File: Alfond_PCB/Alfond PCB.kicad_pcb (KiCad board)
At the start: 4 copper layers, 39 parts, among them J3 Conn_01x05_Pin, J5 USB_B_Micro, P1 PHR-2, SW1 SW_SPDT, U1 DS18B20, U2 STM32U545VETx, U3 MIC5219-3.3YMM, Y1 16MHz

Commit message: Add files via upload
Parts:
- added INA+: PinHeader_1x01_P2.54mm_Vertical, Connector_PinHeader_2.54mm:PinHeader_1x01_P2.54mm_Vertical, F.Cu at (180.5, 77.5)
- added INA-: PinHeader_1x01_P2.54mm_Vertical, Connector_PinHeader_2.54mm:PinHeader_1x01_P2.54mm_Vertical, F.Cu at (186.5, 77.5)
- moved C1 16.3 mm to (224.0, 89.5), turned to 180 degrees
- moved C7 4.03 mm to (214.0, 66.5), turned to -90 degrees
- moved C13 2.00 mm to (174.0, 89.0)
- moved C6 1.50 mm to (212.5, 70.5)
- moved C4 1.12 mm to (213.5, 78.5)
- moved R5 0.50 mm to (221.0, 63.0)
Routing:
- net +3.3V: track 64.8 -> 267.5 mm, vias 1 -> 11
- net GND: track 222.6 -> 320.3 mm, vias 6 -> 12
- net /I2C1_SDA: track 0.00 -> 75.3 mm, vias 0 -> 3
- net /I2C1_SCL: track 0.00 -> 75.0 mm, vias 0 -> 3
- net /UART5_RX: track 0.00 -> 70.9 mm, vias 0 -> 1
- net /UART5_TX: track 0.00 -> 69.4 mm, vias 0 -> 3
- net /GPIO_SLEEP_XBEE: track 0.00 -> 60.2 mm, vias 0 -> 3
- net /UART4_TX: track 0.00 -> 41.7 mm, vias 0 -> 2
- net /INA+: track 0.00 -> 32.6 mm, vias 0 -> 3
- net /I2C3_SDA: track 0.00 -> 28.5 mm, vias 0 -> 4
- net /I2C3_SCL: track 0.00 -> 27.9 mm, vias 0 -> 2
- net /INA-: track 0.00 -> 27.3 mm, vias 0 -> 2
- net /NRST: track 47.9 -> 61.2 mm, vias 3 -> 4
- net Net-(D4-A): track 10.9 -> 15.0 mm, vias 0 -> 1
- net /GPIO_INPUT_Button: track 13.1 -> 15.0 mm
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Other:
- board outline added: 84.5 x 50 mm

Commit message: Removed layers
Had extra copper layers that weren't used, and forgot to comment on the last push, but it was creating a fully connected pcb
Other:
- copper layers 4 -> 2
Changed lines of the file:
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@@
 	(layers
 		(0 "F.Cu" signal)
-		(1 "In1.Cu" signal)
-		(2 "In2.Cu" signal)
 		(31 "B.Cu" power)
 		(34 "B.Paste" user)
@@
 			)
 			(layer "dielectric 1"
-				(type "prepreg")
-				(thickness 0.1)
-				(material "FR4")
-				(epsilon_r 4.5)
-				(loss_tangent 0.02)
-			)
-			(layer "In1.Cu"
-				(type "copper")
-				(thickness 0.035)
-			)
-			(layer "dielectric 2"
-				(type "prepreg")
-				(thickness 1.24)
-				(material "FR4")
-				(epsilon_r 4.5)
-				(loss_tangent 0.02)
-			)
-			(layer "In2.Cu"
-				(type "copper")
-				(thickness 0.035)
-			)
-			(layer "dielectric 3"
-				(type "prepreg")
-				(thickness 0.1)
+				(type "core")
+				(thickness 1.51)
 				(material "FR4")
 				(epsilon_r 4.5)
@@
 			(plot_on_all_layers_selection 0x0000000_00000000)
 			(disableapertmacros no)
-			(usegerberextensions no)
+			(usegerberextensions yes)
 			(usegerberattributes yes)
 			(usegerberadvancedattributes yes)
-			(creategerberjobfile yes)
+			(creategerberjobfile no)
 			(dashed_line_dash_ratio 12.000000)
 			(dashed_line_gap_ratio 3.000000)
@@
 			(plotinvisibletext no)
 			(sketchpadsonfab no)
-			(subtractmaskfromsilk no)
+			(subtractmaskfromsilk yes)
 			(outputformat 1)
 			(mirror no)
-			(drillshape 1)
+			(drillshape 0)
 			(scaleselection 1)
-			(outputdirectory "")
+			(outputdirectory "C:/Users/mpica/Downloads/Gerber_Files_Alfond_PCB/")
 		)
 	)

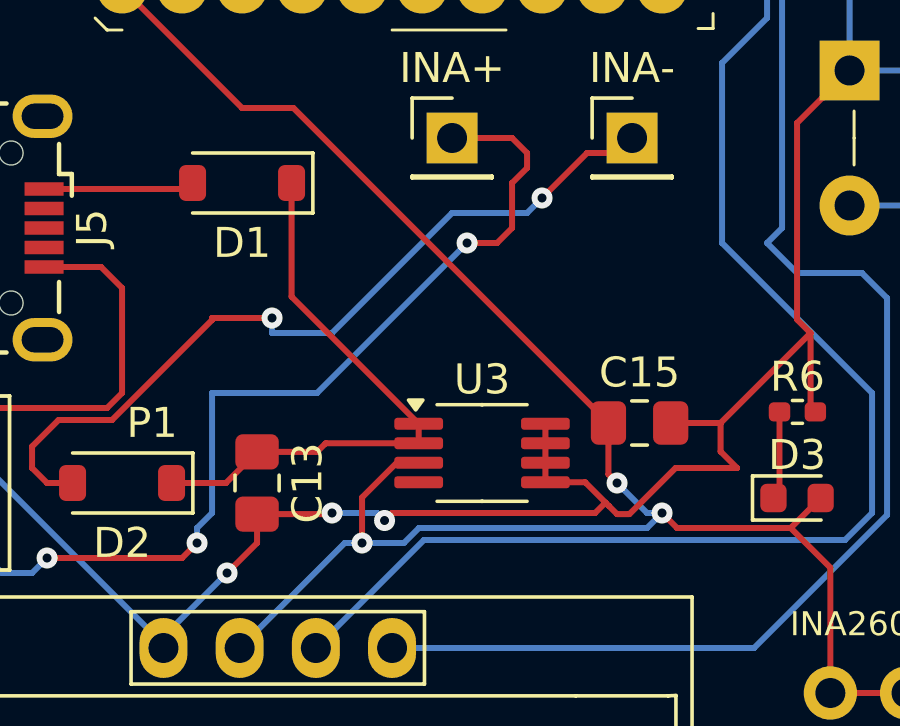
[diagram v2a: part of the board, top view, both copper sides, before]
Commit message: Update to PCB and Footprints
The PCB was updated to the correct MIC ordered from Digikey, and the footprint was added to the footprint folders.
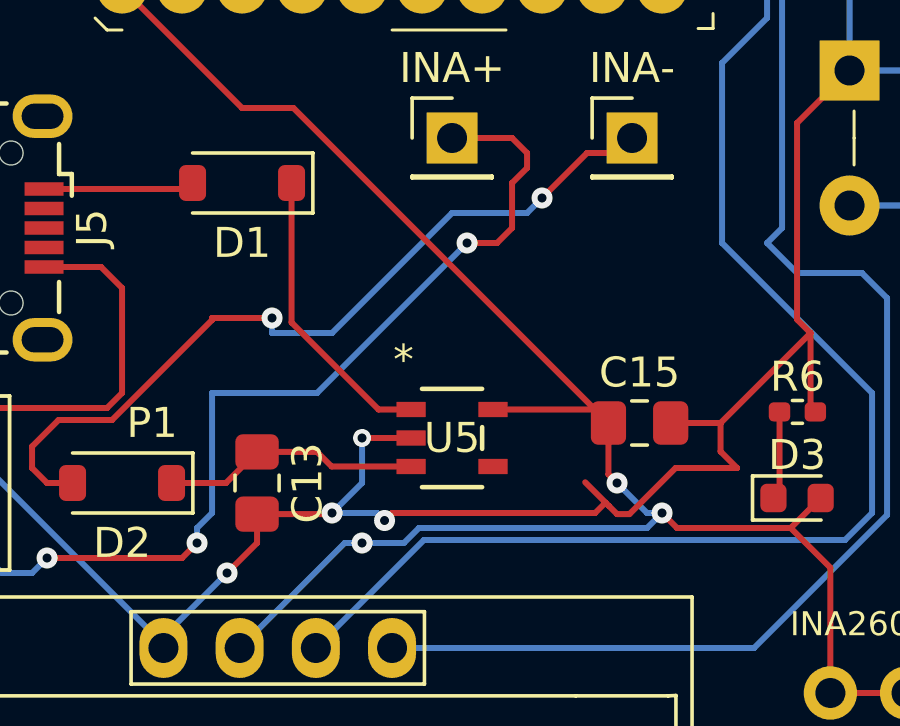
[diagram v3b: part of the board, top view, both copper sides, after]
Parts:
- removed U3: MIC5219-3.3YMM, Package_SO:MSOP-8_3x3mm_P0.65mm
- added U5: MIC5219-3.3YM5-TR, Mics:SOT-23-5_M5_MCH, F.Cu at (180.5, 87.5)
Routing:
- net GND: track 320.3 -> 321.6 mm, vias 12 -> 13
- net Net-(D1-K): track 19.2 -> 18.5 mm

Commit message: fixed few errors
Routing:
- net GND: track 321.6 -> 320.7 mm
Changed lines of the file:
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@@
 		(tags "MIC5219-3.3YM5-TR ")
 		(property "Reference" "U5"
-			(at 0 0 0)
+			(at 0 -3 0)
 			(unlocked yes)
 			(layer "F.SilkS")
@@
 		)
 		(fp_text user "*"
-			(at -1.61925 -2.601 0)
-			(layer "F.SilkS")
-			(effects
-				(font
-					(size 1 1)
-					(thickness 0.15)
-				)
-			)
-		)
-		(fp_text user "*"
-			(at -1.61925 -2.601 0)
-			(unlocked yes)
-			(layer "F.SilkS")
-			(effects
-				(font
-					(size 1 1)
-					(thickness 0.15)
-				)
-			)
-		)
-		(fp_text user "*"
 			(at -0.6223 -1.5088 0)
 			(unlocked yes)
@@
 		)
 		(pad "" smd roundrect
-			(at -0.3625 0)
+			(at -0.5 0)
 			(size 0.41 0.27)
 			(layers "F.Paste")
@@
 		)
 		(pad "" smd roundrect
-			(at 0.3625 0)
+			(at 0.5 0)
 			(size 0.41 0.27)
 			(layers "F.Paste")
@@
 		)
 		(pad "1" smd roundrect
-			(at -0.3375 0)
+			(at -0.5 0)
 			(size 0.575 0.3)
 			(layers "F.Cu" "F.Mask")
@@
 		)
 		(pad "2" smd roundrect
-			(at 0.3375 0)
+			(at 0.5 0)
 			(size 0.575 0.3)
 			(layers "F.Cu" "F.Mask")
@@
 	)
 	(segment
+		(start 189.45 87.95)
+		(end 189.45 87)
+		(width 0.2)
+		(layer "F.Cu")
+		(net 2)
+	)
+	(segment
 		(start 214 67.0675)
 		(end 214 68.39)
@@
 	)
 	(segment
+		(start 186 90.0375)
+		(end 186.4125 90.0375)
+		(width 0.2)
+		(layer "F.Cu")
+		(net 2)
+	)
+	(segment
 		(start 212.734 93.734)
 		(end 213 94)
@@
 	)
 	(segment
+		(start 185.615625 89.653125)
+		(end 186 90.0375)
+		(width 0.2)
+		(layer "F.Cu")
+		(net 2)
+	)
+	(segment
 		(start 216.325 77)
 		(end 218.5 77)
@@
 	)
 	(segment
-		(start 186.4125 90.0375)
-		(end 187.95 88.5)
-		(width 0.2)
-		(layer "F.Cu")
-		(net 2)
-	)
-	(segment
 		(start 226.248529 92.1)
 		(end 224.1 92.1)
@@
 	)
 	(segment
+		(start 186.4125 90.0375)
+		(end 187.95 88.5)
+		(width 0.2)
+		(layer "F.Cu")
+		(net 2)
+	)
+	(segment
 		(start 185.615625 89.653125)
 		(end 185.26875 90)
@@
 	)
 	(segment
-		(start 187.95 88.5)
-		(end 190 88.5)
-		(width 0.2)
-		(layer "F.Cu")
-		(net 2)
-	)
-	(segment
 		(start 229.4325 84.5)
 		(end 229.4325 88.418971)
@@
 	)
 	(segment
-		(start 190 88.5)
-		(end 189.45 87.95)
-		(width 0.2)
-		(layer "F.Cu")
-		(net 2)
-	)
-	(segment
 		(start 194 58.5)
 		(end 194 58)
@@
 	)
 	(segment
+		(start 216 93)
+		(end 214.8375 93)
+		(width 0.2)
+		(layer "F.Cu")
+		(net 2)
+	)
+	(segment
 		(start 210.5 77.365)
 		(end 211.0675 77.9325)
@@
 	)
 	(segment
-		(start 216 93)
-		(end 214.8375 93)
-		(width 0.2)
-		(layer "F.Cu")
-		(net 2)
-	)
-	(segment
-		(start 184.9375 88.975)
-		(end 185.73125 89.76875)
+		(start 218 80.34259)
+		(end 218 80)
 		(width 0.2)
 		(layer "F.Cu")
@@
 	)
 	(segment
-		(start 218 80.34259)
-		(end 218 80)
+		(start 174 90.0375)
+		(end 176.4625 90.0375)
 		(width 0.2)
 		(layer "F.Cu")
@@
 	)
 	(segment
-		(start 174 90.0375)
-		(end 176.4625 90.0375)
+		(start 187.95 88.5)
+		(end 190 88.5)
 		(width 0.2)
 		(layer "F.Cu")
@@
 	)
 	(segment
-		(start 189.45 87.95)
-		(end 189.45 87)
-		(width 0.2)
-		(layer "F.Cu")
-		(net 2)
-	)
-	(segment
 		(start 192.61 86.63)
 		(end 192.45 86.47)
@@
 	)
 	(segment
-		(start 185.73125 89.76875)
-		(end 186 90.0375)
-		(width 0.2)
-		(layer "F.Cu")
-		(net 2)
-	)
-	(segment
 		(start 174 91)
 		(end 173 92)
@@
 	)
 	(segment
-		(start 186 90.0375)
-		(end 186.4125 90.0375)
-		(width 0.2)
-		(layer "F.Cu")
-		(net 2)
-	)
-	(segment
 		(start 220.5 75)
 		(end 220.5 76)
@@
 		(net 2)
 	)
+	(segment
+		(start 190 88.5)
+		(end 189.45 87.95)
+		(width 0.2)
+		(layer "F.Cu")
+		(net 2)
+	)
 	(via
 		(at 194 58.5)
@@
 	(via
 		(at 177.5 87.5)
-		(size 0.6)
+		(size 0.7)
 		(drill 0.3)
 		(layers "F.Cu" "B.Cu")
@@
 	)
 	(segment
-		(start 213.9025 89.5)
-		(end 212.5 90.9025)
+		(start 215 87)
+		(end 215 84.675)
 		(width 0.2)
 		(layer "F.Cu")
@@
 	)
 	(segment
-		(start 215 87)
-		(end 215 84.675)
+		(start 215 88.4025)
+		(end 213.9025 89.5)
 		(width 0.2)
 		(layer "F.Cu")
@@
 	)
 	(segment
-		(start 215 88.4025)
-		(end 213.9025 89.5)
+		(start 213.9025 89.5)
+		(end 212.5 90.9025)
 		(width 0.2)
 		(layer "F.Cu")
@@
 	)
 	(segment
-		(start 212.5 92.5)
-		(end 213 93)
-		(width 0.2)
+		(start 213 93)
+		(end 214.1625 93)
+		(width 0.3)
 		(layer "F.Cu")
 		(net 5)
 	)
 	(segment
-		(start 213 93)
-		(end 214.1625 93)
-		(width 0.2)
+		(start 212.5 92.5)
+		(end 213 93)
+		(width 0.3)
 		(layer "F.Cu")
 		(net 5)

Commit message: PCB changes
Added text for project name and group members, along with changing capacitor 14 from a footprint that wasn't working with one that is.
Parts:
- C14: value 0.1u -> 100n; footprint Capacitor_SMD:C_01005_0402Metric_Pad0.57x0.30mm_HandSolder -> Capacitor_SMD:C_0402_1005Metric_Pad0.74x0.62mm_HandSolder
- moved C7 2.06 mm to (216.0, 66.0)
- moved C6 2.00 mm to (214.5, 70.5)
- moved C5 1.15 mm to (214.0, 72.5), turned to 180 degrees
- moved C4 1.12 mm to (214.5, 78.0)
- moved C2 1.00 mm to (230.0, 83.5)
- moved C9 0.50 mm to (234.5, 69.0), turned to 0 degrees
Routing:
- net GND: track 320.7 -> 334.0 mm
- net +3.3V: track 267.6 -> 259.5 mm, vias 11 -> 10
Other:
- board text added: "Alfond Data Logger Siddhartha Bajracharya Alex Picard"

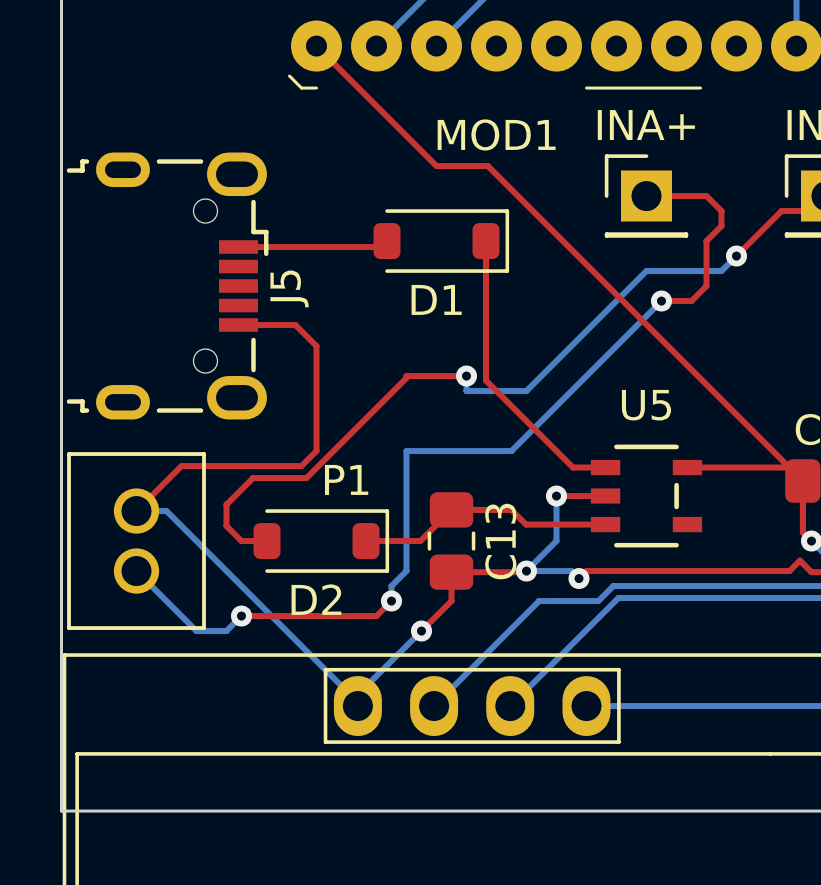
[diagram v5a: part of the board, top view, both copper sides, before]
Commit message: Final PCB Changes
Changed the Schottky diodes to the MAX40200 diodes
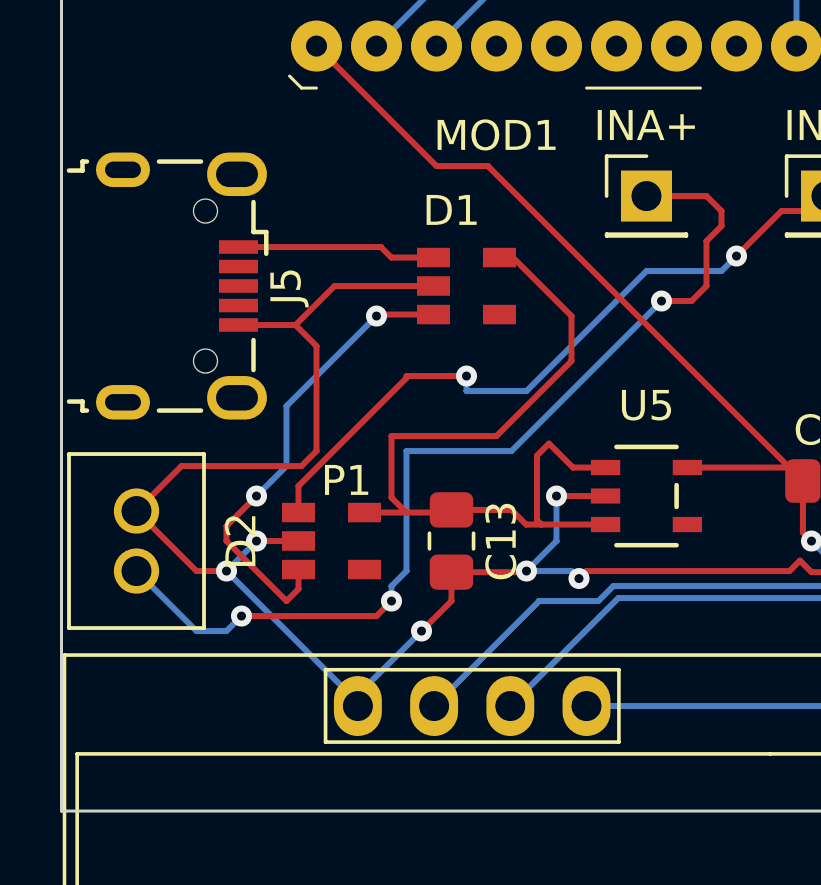
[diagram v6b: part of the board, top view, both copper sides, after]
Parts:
- D1, D2: value D_Schottky -> SOT-23-5; footprint Diode_SMD:D_SOD-123 -> MAX40200AUK_T:SOT-23-5
- moved D1 1.80 mm to (174.5, 80.5), turned to 90 degrees
- moved D2 0.50 mm to (170.0, 89.0), turned to 90 degrees
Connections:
- D1 pad 1: Net-(D1-K) -> /V_USB
- D1 pad 2: /V_USB -> GND
- D2 pad 1: Net-(D1-K) -> /INA-
- D2 pad 2: /INA- -> GND
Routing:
- net EN: track 0.00 -> 15.5 mm, vias 0 -> 2
- net Net-(D1-K): track 18.5 -> 27.9 mm
- net GND: track 334.0 -> 342.0 mm, vias 13 -> 15
- net /INA-: track 27.3 -> 23.2 mm
- net /V_USB: track 5.03 -> 6.64 mm

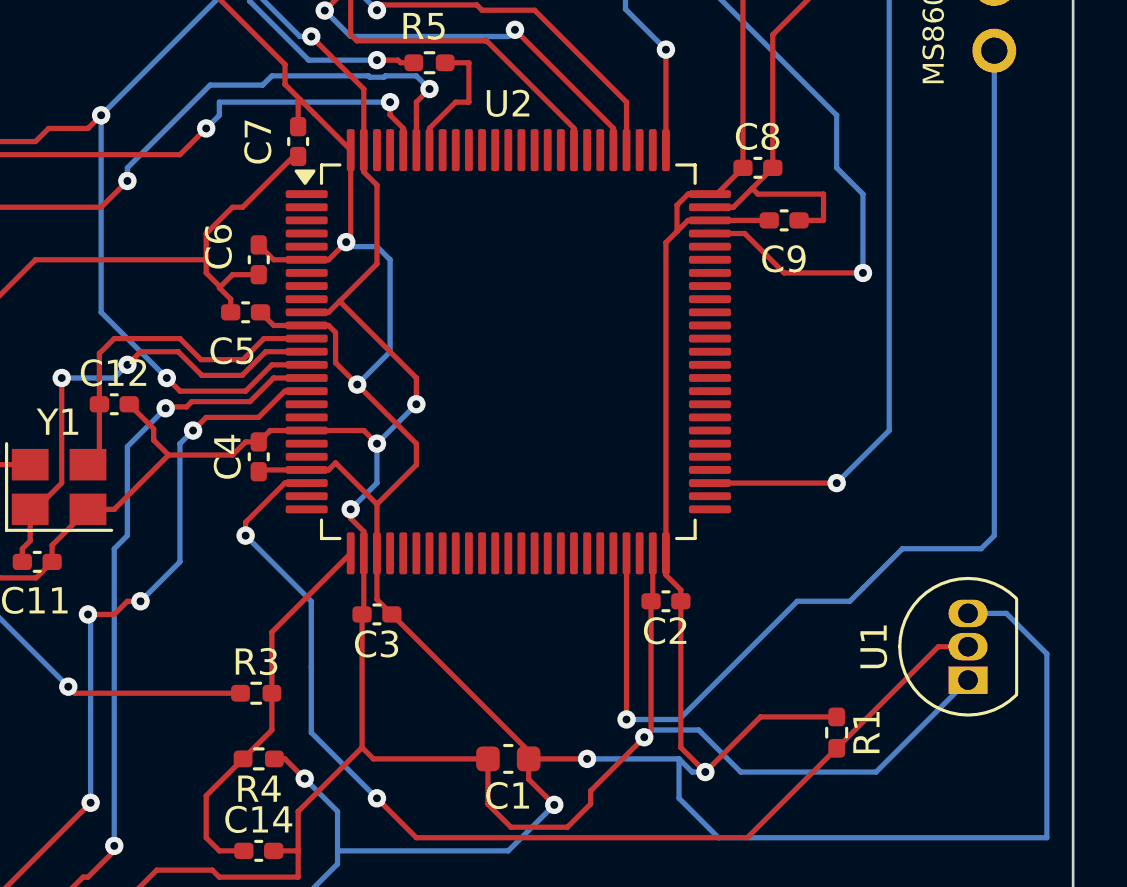
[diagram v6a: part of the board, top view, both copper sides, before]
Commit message: Added test points
Added test points for possible debugging of PCB
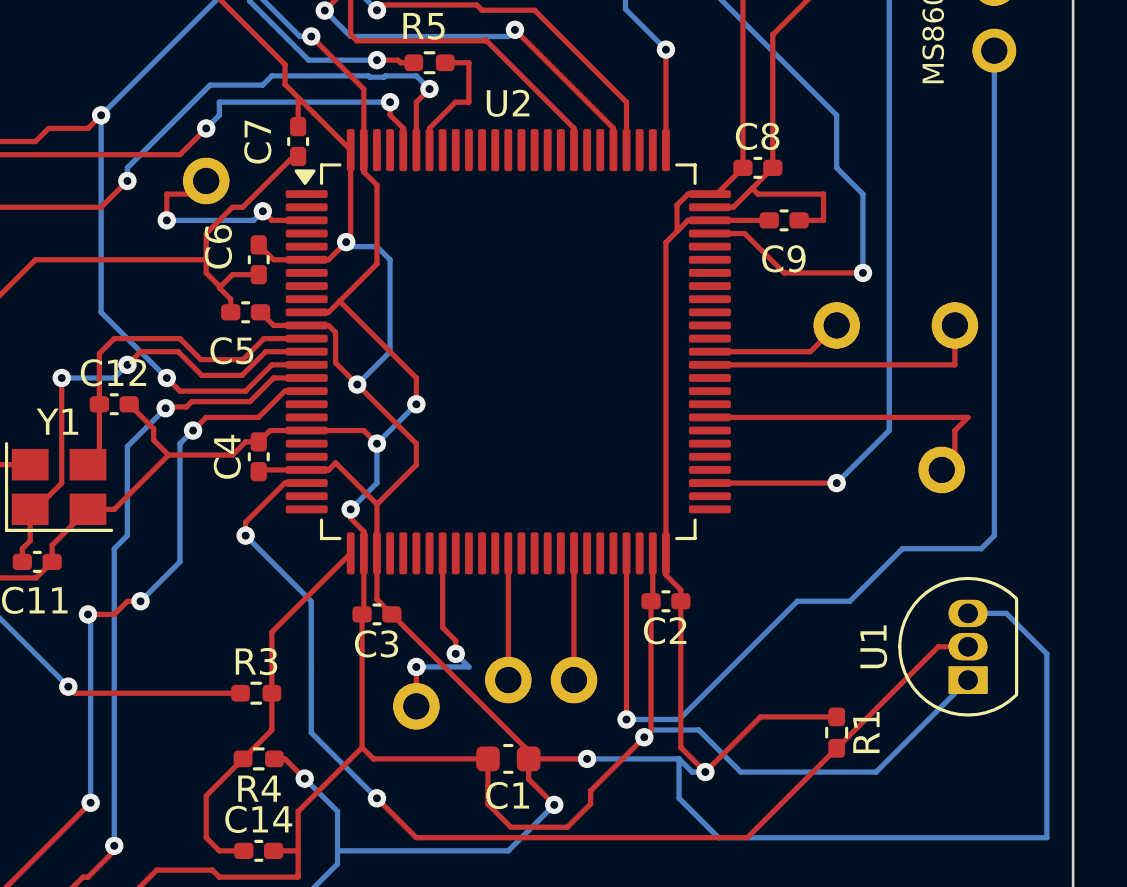
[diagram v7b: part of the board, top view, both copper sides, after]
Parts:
- added ?: , , F.Cu at (212.5, 67.5)
- added ?: , , F.Cu at (236.5, 73.0)
- added ?: , , F.Cu at (224.0, 86.5)
- added ?: , , F.Cu at (241.0, 73.0)
- added ?: , , F.Cu at (220.5, 87.5)
- added ?: , , F.Cu at (240.5, 78.5)
- added ?: , , F.Cu at (226.5, 86.5)
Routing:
- net unconnected-(U2-PD11-Pad58): track 0.00 -> 12.2 mm
- net unconnected-(U2-PD15-Pad62): track 0.00 -> 10.8 mm
- net unconnected-(U2-PE4-Pad3): track 0.00 -> 8.32 mm, vias 0 -> 2
- net unconnected-(U2-PC4-Pad33): track 0.00 -> 8.24 mm, vias 0 -> 2
- net unconnected-(U2-PC6-Pad63): track 0.00 -> 5.24 mm
- net unconnected-(U2-PE7-Pad38): track 0.00 -> 4.83 mm
- net unconnected-(U2-PE12-Pad43): track 0.00 -> 4.83 mm

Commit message: made improvments to pcb
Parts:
- removed U1: DS18B20, Package_TO_SOT_THT:TO-92_Inline
- added ?: , , F.Cu at (241.5, 86.2)
- added ?: , , F.Cu at (241.5, 84.0)
- added ?: , , F.Cu at (241.5, 88.5)
- added H1: MountingHole, MountingHole:MountingHole_2.2mm_M2, F.Cu at (157.8, 48.0)
- added H2: MountingHole, MountingHole:MountingHole_2.2mm_M2, F.Cu at (242.2, 48.2)
- added H3: MountingHole, MountingHole:MountingHole_2.2mm_M2, F.Cu at (158.0, 96.8)
- added H4: MountingHole, MountingHole:MountingHole_2.2mm_M2, F.Cu at (242.5, 96.5)
- C1: footprint Capacitor_SMD:C_0603_1608Metric -> Capacitor_SMD:C_0805_2012Metric_Pad1.18x1.45mm_HandSolder
- C10, C11, C12, C14, C2, C3, C4, C5, C6, C7, C8, C9: footprint Capacitor_SMD:C_0402_1005Metric_Pad0.74x0.62mm_HandSolder -> Capacitor_SMD:C_0805_2012Metric_Pad1.18x1.45mm_HandSolder
- J5: footprint Connector_USB:USB_Micro-B_Wuerth_629105150521 -> Connector_USB:USB_Micro-B_Amphenol_10118193-0001LF_Horizontal
- R1, R3, R4, R5, R6, R7: footprint Resistor_SMD:R_0402_1005Metric_Pad0.72x0.64mm_HandSolder -> Resistor_SMD:R_0603_1608Metric_Pad0.98x0.95mm_HandSolder
- moved J5 7.50 mm to (157.5, 80.7)
- moved P1 6.01 mm to (157.5, 88.8), turned to 90 degrees
- moved C6 1.82 mm to (212.8, 70.0), turned to 180 degrees
- moved C8 1.82 mm to (233.0, 65.2)
- moved C7 1.35 mm to (214.8, 65.5)
- moved C5 1.27 mm to (212.8, 72.2)
- moved C4 1.25 mm to (213.5, 78.8)
- moved C2 0.90 mm to (230.8, 84.0)
- moved C9 0.75 mm to (235.2, 69.0)
- moved C12 0.50 mm to (208.5, 76.0)
- moved R7 0.50 mm to (191.5, 55.0), turned to 0 degrees
- moved C11 0.50 mm to (206.5, 82.2)
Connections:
- U2 pad 47: /I2C2_SDA -> /I2C2_SCL
- U2 pad 53: /I2C2_SCL -> /I2C2_SDA
- U2 pad 95: /I2C1_SDA -> /I2C1_SCL
- U2 pad 96: /I2C1_SCL -> /I2C1_SDA
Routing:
- net /I2C2_SDA: track 41.7 -> 24.2 mm
- net /I2C2_SCL: track 28.7 -> 43.4 mm
- net GND: track 342.0 -> 354.6 mm, vias 15 -> 17
- net /V_USB: track 6.64 -> 13.3 mm
- net /INA+: track 32.6 -> 39.2 mm
- net +3.3V: track 259.5 -> 262.5 mm
- net /I2C1_SDA: track 75.3 -> 73.0 mm
- net /I2C1_SCL: track 75.0 -> 77.1 mm
- net unconnected-(U2-PE4-Pad3): track 8.32 -> 10.1 mm
- net /HSE_OUT: track 18.2 -> 19.8 mm
- net /PWR_LED_K2: track 1.47 -> 2.94 mm
- net /HSE_IN: track 13.2 -> 14.3 mm
- net /UART4_TX: track 41.7 -> 40.8 mm
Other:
- board size 84.5 x 50 mm -> 91.2 x 54.2 mm
